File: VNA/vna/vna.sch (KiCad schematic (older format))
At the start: 2 parts, among them J1 Conn_Coaxial, J2 Conn_Coaxial

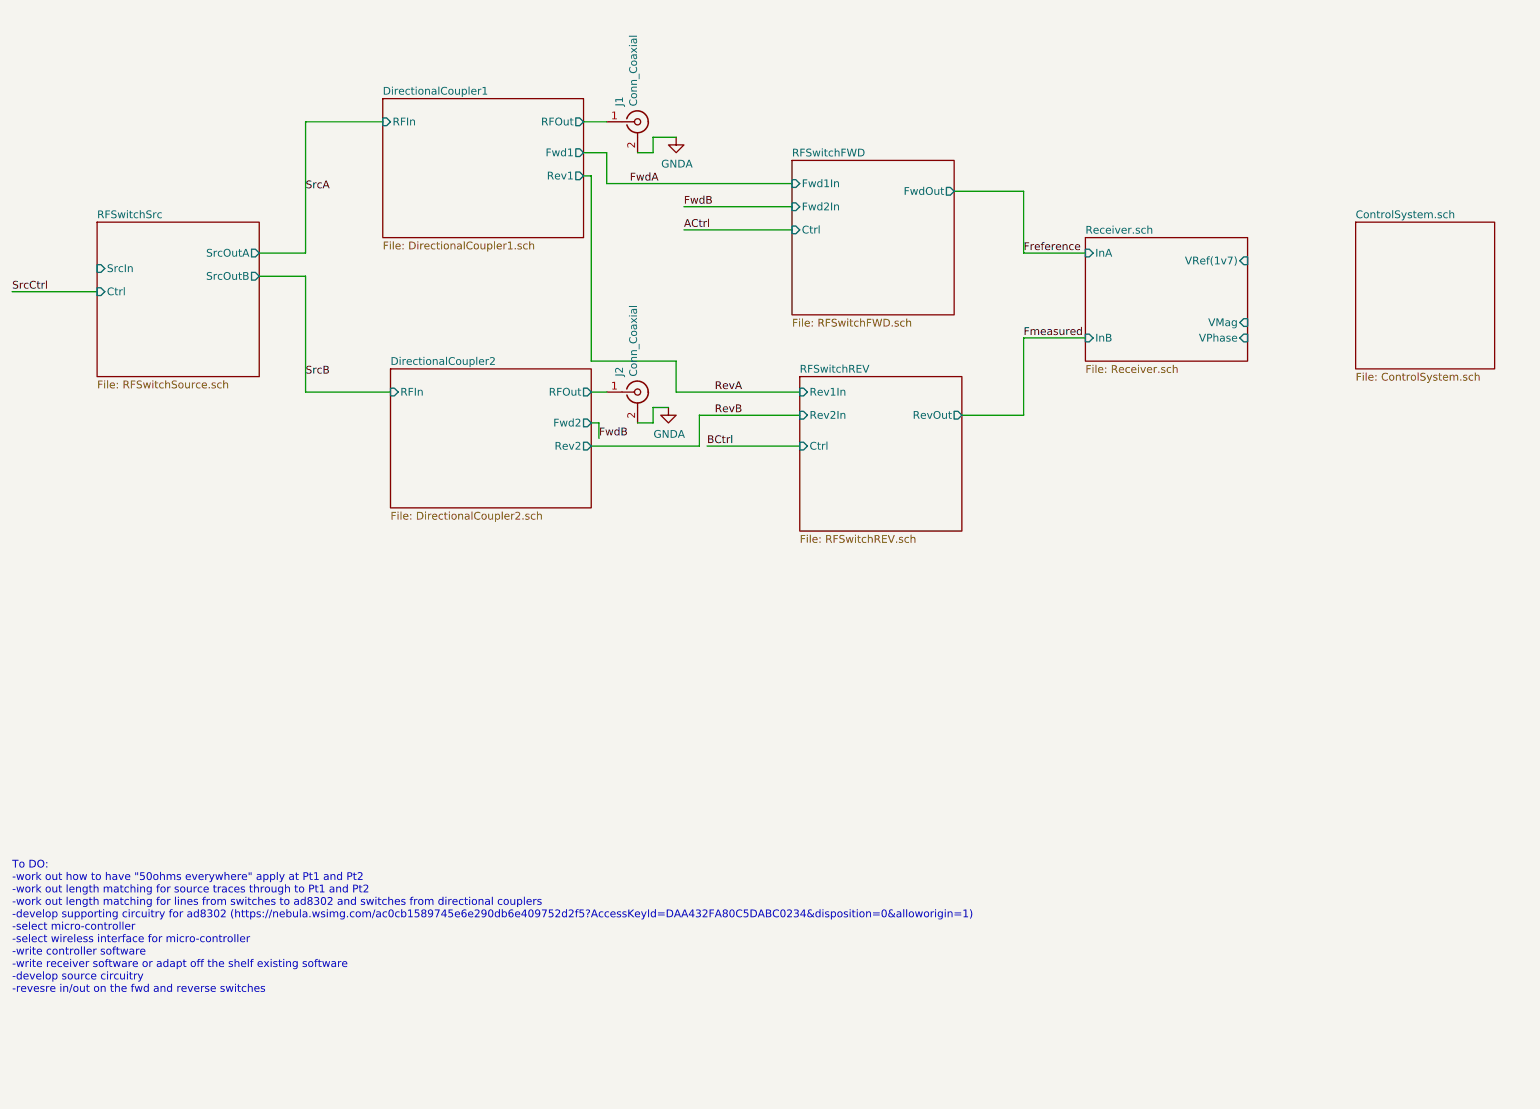
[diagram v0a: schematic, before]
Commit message: power and rf src blocks added
battery managemet and rf source heirachical schematics have been added.

these schematics are still empty however will server as a test for visual diff.
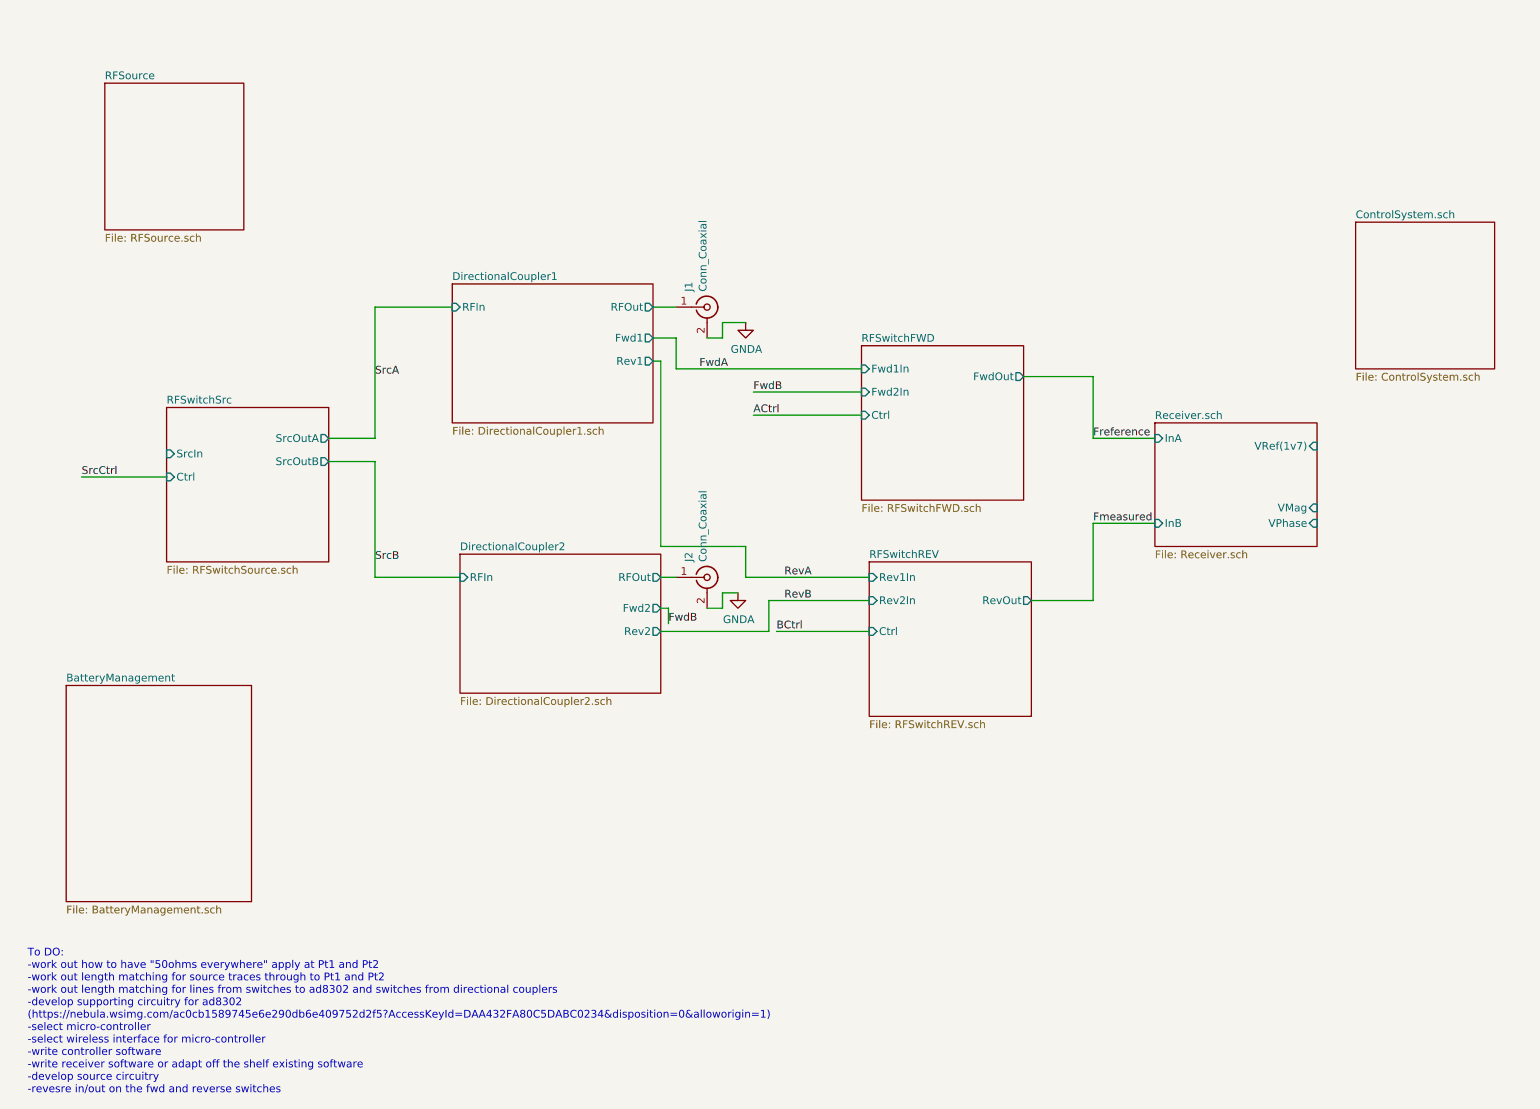
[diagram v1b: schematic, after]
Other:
- note added: "To DO:\n-work out how to have "50ohms everywhere" apply at Pt1 and Pt2\n-work out length matching for source traces through to Pt1 and Pt2\n-work out length matching for lines from switches to ad8302 and switches from directional couplers\n-develop supporting circuitry for ad8302 \n(https://nebula.wsimg.com/ac0cb1589745e6e290db6e409752d2f5?AccessKeyId=DAA432FA80C5DABC0234&disposition=0&alloworigi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"
- note removed: "To DO:\n-work out how to have "50ohms everywhere" apply at Pt1 and Pt2\n-work out length matching for source traces through to Pt1 and Pt2\n-work out length matching for lines from switches to ad8302 and switches from directional couplers\n-develop supporting circuitry for ad8302 (https://nebula.wsimg.com/ac0cb1589745e6e290db6e409752d2f5?AccessKeyId=DAA432FA80C5DABC0234&disposition=0&alloworigin=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"
- moved on the sheet: J1, J2
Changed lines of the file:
@@
 $Descr A4 11693 8268
 encoding utf-8
-Sheet 1 8
+Sheet 1 9
 Title "Vector Network Analyser"
 Date "2019-04-24"
@@
 L Connector:Conn_Coaxial J1
 U 1 1 5CC13FA2
-P 4650 1250
-F 0 "J1" V 4532 1350 50  0000 L CNN
-F 1 "Conn_Coaxial" V 4623 1350 50  0000 L CNN
-F 2 "" H 4650 1250 50  0001 C CNN
-F 3 " ~" H 4650 1250 50  0001 C CNN
-	1    4650 1250
-	1    0    0    -1
-$EndComp
-Text Notes 600  6900 0    50   ~ 0
-To DO:\n-work out how to have "50ohms everywhere" apply at Pt1 and Pt2\n-work out length matching for source traces through to Pt1 and Pt2\n-work out length matching for lines from switches to ad8302 and switches from directional couplers\n-develop supporting circuitry for ad8302 (https://nebula.wsimg.com/ac0cb1589745e6e290db6e409752d2f5?AccessKeyId=DAA432FA80C5DABC0234&disposition=0&alloworigin=1)\n-select micro-controller\n-select wireless interface for micro-controller\n-write controller software\n-write receiver software or adapt off the shelf existing software\n-develop source circuitry\n-revesre in/out on the fwd and reverse switches
-$Sheet
-S 3000 1100 1300 900
+P 5100 2450
+F 0 "J1" V 4982 2550 50  0000 L CNN
+F 1 "Conn_Coaxial" V 5073 2550 50  0000 L CNN
+F 2 "" H 5100 2450 50  0001 C CNN
+F 3 " ~" H 5100 2450 50  0001 C CNN
+	1    5100 2450
+	1    0    0    -1
+$EndComp
+Text Notes 700  7550 0    50   ~ 0
+To DO:\n-work out how to have "50ohms everywhere" apply at Pt1 and Pt2\n-work out length matching for source traces through to Pt1 and Pt2\n-work out length matching for lines from switches to ad8302 and switches from directional couplers\n-develop supporting circuitry for ad8302 \n(https://nebula.wsimg.com/ac0cb1589745e6e290db6e409752d2f5?AccessKeyId=DAA432FA80C5DABC0234&disposition=0&alloworigin=1)\n-select micro-controller\n-select wireless interface for micro-controller\n-write controller software\n-write receiver software or adapt off the shelf existing software\n-develop source circuitry\n-revesre in/out on the fwd and reverse switches
+$Sheet
+S 3450 2300 1300 900
 U 5CC1CC6B
 F0 "DirectionalCoupler1" 50
 F1 "DirectionalCoupler1.sch" 50
-F2 "RFIn" I L 3000 1250 50
-F3 "RFOut" O R 4300 1250 50
-F4 "Fwd1" O R 4300 1450 50
-F5 "Rev1" O R 4300 1600 50
-$EndSheet
-$Sheet
-S 3050 2850 1300 900
+F2 "RFIn" I L 3450 2450 50
+F3 "RFOut" O R 4750 2450 50
+F4 "Fwd1" O R 4750 2650 50
+F5 "Rev1" O R 4750 2800 50
+$EndSheet
+$Sheet
+S 3500 4050 1300 900
 U 5CC6A089
 F0 "DirectionalCoupler2" 50
 F1 "DirectionalCoupler2.sch" 50
-F2 "RFIn" I L 3050 3000 50
-F3 "RFOut" O R 4350 3000 50
-F4 "Fwd2" O R 4350 3200 50
-F5 "Rev2" O R 4350 3350 50
-$EndSheet
-$Sheet
-S 1150 1900 1050 1000
+F2 "RFIn" I L 3500 4200 50
+F3 "RFOut" O R 4800 4200 50
+F4 "Fwd2" O R 4800 4400 50
+F5 "Rev2" O R 4800 4550 50
+$EndSheet
+$Sheet
+S 1600 3100 1050 1000
 U 5CC6DDE1
 F0 "RFSwitchSrc" 50
 F1 "RFSwitchSource.sch" 50
-F2 "SrcIn" I L 1150 2200 50
-F3 "SrcOutA" O R 2200 2100 50
-F4 "SrcOutB" O R 2200 2250 50
-F5 "Ctrl" I L 1150 2350 50
-$EndSheet
-$Sheet
-S 5650 1500 1050 1000
+F2 "SrcIn" I L 1600 3400 50
+F3 "SrcOutA" O R 2650 3300 50
+F4 "SrcOutB" O R 2650 3450 50
+F5 "Ctrl" I L 1600 3550 50
+$EndSheet
+$Sheet
+S 6100 2700 1050 1000
 U 5CCA83E4
 F0 "RFSwitchFWD" 50
 F1 "RFSwitchFWD.sch" 50
-F2 "Ctrl" I L 5650 1950 50
-F3 "FwdOut" O R 6700 1700 50
-F4 "Fwd1In" I L 5650 1650 50
-F5 "Fwd2In" I L 5650 1800 50
-$EndSheet
-Wire Wire Line
-	2200 2100 2500 2100
-Wire Wire Line
-	2500 2100 2500 1250
-Wire Wire Line
-	2500 1250 3000 1250
-Wire Wire Line
-	2200 2250 2500 2250
-Wire Wire Line
-	2500 2250 2500 3000
-Wire Wire Line
-	2500 3000 3050 3000
-Wire Wire Line
-	4300 1250 4450 1250
-Wire Wire Line
-	4350 3000 4450 3000
-$Sheet
-S 5700 2900 1050 1000
+F2 "Ctrl" I L 6100 3150 50
+F3 "FwdOut" O R 7150 2900 50
+F4 "Fwd1In" I L 6100 2850 50
+F5 "Fwd2In" I L 6100 3000 50
+$EndSheet
+Wire Wire Line
+	2650 3300 2950 3300
+Wire Wire Line
+	2950 3300 2950 2450
+Wire Wire Line
+	2950 2450 3450 2450
+Wire Wire Line
+	2650 3450 2950 3450
+Wire Wire Line
+	2950 3450 2950 4200
+Wire Wire Line
+	2950 4200 3500 4200
+Wire Wire Line
+	4750 2450 4900 2450
+Wire Wire Line
+	4800 4200 4900 4200
+$Sheet
+S 6150 4100 1050 1000
 U 5CCA993F
 F0 "RFSwitchREV" 50
 F1 "RFSwitchREV.sch" 50
-F2 "Ctrl" I L 5700 3350 50
-F3 "RevOut" O R 6750 3150 50
-F4 "Rev1In" I L 5700 3000 50
-F5 "Rev2In" I L 5700 3150 50
-$EndSheet
-Text Label 2500 2900 0    50   ~ 0
+F2 "Ctrl" I L 6150 4550 50
+F3 "RevOut" O R 7200 4350 50
+F4 "Rev1In" I L 6150 4200 50
+F5 "Rev2In" I L 6150 4350 50
+$EndSheet
+Text Label 2950 4100 0    50   ~ 0
 SrcB
-Text Label 2500 1700 0    50   ~ 0
+Text Label 2950 2900 0    50   ~ 0
 SrcA
 Wire Wire Line
-	4300 1450 4450 1450
-Wire Wire Line
-	4450 1450 4450 1650
-Wire Wire Line
-	4450 1650 5650 1650
-Wire Wire Line
-	4350 3350 5050 3350
-Wire Wire Line
-	5050 3350 5050 3150
-Wire Wire Line
-	5050 3150 5700 3150
-Wire Wire Line
-	4300 1600 4350 1600
-Wire Wire Line
-	4350 1600 4350 2800
-Wire Wire Line
-	4350 2800 4900 2800
-Wire Wire Line
-	4900 2800 4900 3000
-Wire Wire Line
-	4900 3000 5700 3000
-Wire Wire Line
-	4350 3200 4400 3200
-Wire Wire Line
-	4400 3200 4400 3300
+	4750 2650 4900 2650
+Wire Wire Line
+	4900 2650 4900 2850
+Wire Wire Line
+	4900 2850 6100 2850
+Wire Wire Line
+	4800 4550 5500 4550
+Wire Wire Line
+	5500 4550 5500 4350
+Wire Wire Line
+	5500 4350 6150 4350
+Wire Wire Line
+	4750 2800 4800 2800
+Wire Wire Line
+	4800 2800 4800 4000
+Wire Wire Line
+	4800 4000 5350 4000
+Wire Wire Line
+	5350 4000 5350 4200
+Wire Wire Line
+	5350 4200 6150 4200
+Wire Wire Line
+	4800 4400 4850 4400
+Wire Wire Line
+	4850 4400 4850 4500
 $Comp
 L power:GNDA #PWR?
 U 1 1 5CCAEFF7
-P 4900 1350
-F 0 "#PWR?" H 4900 1100 50  0001 C CNN
-F 1 "GNDA" H 4905 1177 50  0000 C CNN
-F 2 "" H 4900 1350 50  0001 C CNN
-F 3 "" H 4900 1350 50  0001 C CNN
-	1    4900 1350
+P 5350 2550
+F 0 "#PWR?" H 5350 2300 50  0001 C CNN
+F 1 "GNDA" H 5355 2377 50  0000 C CNN
+F 2 "" H 5350 2550 50  0001 C CNN
+F 3 "" H 5350 2550 50  0001 C CNN
+	1    5350 2550
 	1    0    0    -1
 $EndComp
@@
 L power:GNDA #PWR?
 U 1 1 5CCAF63F
-P 4850 3100
-F 0 "#PWR?" H 4850 2850 50  0001 C CNN
-F 1 "GNDA" H 4855 2927 50  0000 C CNN
-F 2 "" H 4850 3100 50  0001 C CNN
-F 3 "" H 4850 3100 50  0001 C CNN
-	1    4850 3100
-	1    0    0    -1
-$EndComp
-Wire Wire Line
-	4650 1450 4750 1450
-Wire Wire Line
-	4750 1450 4750 1350
-Wire Wire Line
-	4750 1350 4900 1350
-Wire Wire Line
-	4750 3200 4750 3100
-Wire Wire Line
-	4750 3100 4850 3100
-Text Label 4600 1650 0    50   ~ 0
+P 5300 4300
+F 0 "#PWR?" H 5300 4050 50  0001 C CNN
+F 1 "GNDA" H 5305 4127 50  0000 C CNN
+F 2 "" H 5300 4300 50  0001 C CNN
+F 3 "" H 5300 4300 50  0001 C CNN
+	1    5300 4300
+	1    0    0    -1
+$EndComp
+Wire Wire Line
+	5100 2650 5200 2650
+Wire Wire Line
+	5200 2650 5200 2550
+Wire Wire Line
+	5200 2550 5350 2550
+Wire Wire Line
+	5200 4400 5200 4300
+Wire Wire Line
+	5200 4300 5300 4300
+Text Label 5050 2850 0    50   ~ 0
 FwdA
-Text Label 4950 1800 0    50   ~ 0
+Text Label 5400 3000 0    50   ~ 0
 FwdB
 Wire Wire Line
-	4950 1800 5650 1800
-Text Label 5150 3000 0    50   ~ 0
+	5400 3000 6100 3000
+Text Label 5600 4200 0    50   ~ 0
 RevA
-Text Label 5150 3150 0    50   ~ 0
+Text Label 5600 4350 0    50   ~ 0
 RevB
 $Sheet
-S 7550 2000 1050 800
+S 8000 3200 1050 800
 U 5CCB994F
 F0 "Receiver.sch" 50
 F1 "Receiver.sch" 50
-F2 "InA" I L 7550 2100 50
-F3 "VRef(1v7)" I R 8600 2150 50
-F4 "VPhase" I R 8600 2650 50
-F5 "VMag" I R 8600 2550 50
-F6 "InB" I L 7550 2650 50
-$EndSheet
-Wire Wire Line
-	6700 1700 7150 1700
-Wire Wire Line
-	7150 1700 7150 2100
-Wire Wire Line
-	7150 2100 7550 2100
-Wire Wire Line
-	6750 3150 7150 3150
-Wire Wire Line
-	7150 3150 7150 2650
-Wire Wire Line
-	7150 2650 7550 2650
-Wire Wire Line
-	4650 3200 4750 3200
+F2 "InA" I L 8000 3300 50
+F3 "VRef(1v7)" I R 9050 3350 50
+F4 "VPhase" I R 9050 3850 50
+F5 "VMag" I R 9050 3750 50
+F6 "InB" I L 8000 3850 50
+$EndSheet
+Wire Wire Line
+	7150 2900 7600 2900
+Wire Wire Line
+	7600 2900 7600 3300
+Wire Wire Line
+	7600 3300 8000 3300
+Wire Wire Line
+	7200 4350 7600 4350
+Wire Wire Line
+	7600 4350 7600 3850
+Wire Wire Line
+	7600 3850 8000 3850
+Wire Wire Line
+	5100 4400 5200 4400
 $Comp
 L Connector:Conn_Coaxial J2
 U 1 1 5CC17996
-P 4650 3000
-F 0 "J2" V 4532 3100 50  0000 L CNN
-F 1 "Conn_Coaxial" V 4623 3100 50  0000 L CNN
-F 2 "" H 4650 3000 50  0001 C CNN
-F 3 " ~" H 4650 3000 50  0001 C CNN
-	1    4650 3000
-	1    0    0    -1
-$EndComp
-Text Label 4400 3300 0    50   ~ 0
+P 5100 4200
+F 0 "J2" V 4982 4300 50  0000 L CNN
+F 1 "Conn_Coaxial" V 5073 4300 50  0000 L CNN
+F 2 "" H 5100 4200 50  0001 C CNN
+F 3 " ~" H 5100 4200 50  0001 C CNN
+	1    5100 4200
+	1    0    0    -1
+$EndComp
+Text Label 4850 4500 0    50   ~ 0
 FwdB
-Text Label 7150 2650 0    50   ~ 0
+Text Label 7600 3850 0    50   ~ 0
 Fmeasured
-Text Label 7150 2100 0    50   ~ 0
+Text Label 7600 3300 0    50   ~ 0
 Freference
 Wire Wire Line
-	5650 1950 4950 1950
-Wire Wire Line
-	5700 3350 5100 3350
-Wire Wire Line
-	1150 2350 600  2350
-Text Label 600  2350 0    50   ~ 0
+	6100 3150 5400 3150
+Wire Wire Line
+	6150 4550 5550 4550
+Wire Wire Line
+	1600 3550 1050 3550
+Text Label 1050 3550 0    50   ~ 0
 SrcCtrl
-Text Label 4950 1950 0    50   ~ 0
+Text Label 5400 3150 0    50   ~ 0
 ACtrl
-Text Label 5100 3350 0    50   ~ 0
+Text Label 5550 4550 0    50   ~ 0
 BCtrl
 $Sheet
@@
 F1 "ControlSystem.sch" 50
 $EndSheet
+$Sheet
+S 1200 1000 900  950
+U 5CDF14FF
+F0 "RFSource" 50
+F1 "RFSource.sch" 50
+$EndSheet
+$Sheet
+S 950  4900 1200 1400
+U 5CDF1C56
+F0 "BatteryManagement" 50
+F1 "BatteryManagement.sch" 50
+$EndSheet
 $EndSCHEMATC
